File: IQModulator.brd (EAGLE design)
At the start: 100 x 80 mm, 122 parts, among them IC1 LM340S, IC2 OP470D, IC3 4539D, IC5 FT232RL-FULLSSOP, IC6 74AC74D, IC7 SI5351A_DEVICE_SMD, IC8 MEGA8-AI, Q1 16MHz, Q2 25MHz, X1 KLBR4

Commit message: Filter + Lib
All Filters designed+ Eagle Lib extended
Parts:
- removed R20, R21, R24, R25: 45, resistor:R0805
- added IC4: SN74CBTLV3253D, _Bachelor-IQModulator:SO16
- C28, C30: value (none) -> 2.2n
- C29, C36, C38: value (none) -> 3.3n
- C31: value (none) -> 100p
- C37, C44, C46: value (none) -> 6.8n
- C39: value (none) -> 150p
- C45: value (none) -> 10n
- C47: value (none) -> 220p
- L11, L12: value (none) -> 4.7u
- L13, L14: value (none) -> 10u
- L15, L16: value (none) -> 15u
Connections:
- removed net N$24: C9.-, R20.1
- removed net N$25: C10.-, R21.1
- removed net N$38: C12.-, R25.1
- removed net N$40: C11.-, R24.1
- new net VDD: IC4.16
- new net VSS: IC4.8
- net -I: now also C12.-, IC4.13, IC4.3; no longer IC3.13, IC3.3, R25.2
- net -Q: now also C10.-, IC4.12, IC4.4; no longer IC3.12, IC3.4, R21.2
- net CLK1: now also IC4.14; no longer IC3.14
- net CLK2: now also IC4.2; no longer IC3.2
- net GND: now also IC4.1, IC4.15; no longer IC3.1, IC3.15
- net I: now also C11.-, IC4.10, IC4.6; no longer IC3.10, IC3.6, R24.2
- net N$16: now also IC4.7; no longer IC3.7
- net N$17: now also IC4.9; no longer IC3.9
- net Q: now also C9.-, IC4.11, IC4.5; no longer IC3.11, IC3.5, R20.2

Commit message: PA+ Relais
Added last changes in the main schematic
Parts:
- removed C49: 100n, resistor:C0805
- removed IC3: 4539D, 45xx:SO16
- added C61: 100n, resistor:C0805
- added C62: 4.7u, resistor:C0805
- added C63: 100n, _Bachelor-IQModulator:C0805
- added D1, D2, D3, D4, D5, D6, D7, D8: (no value), diode:DO214AA
- added L19, L20, L22: 10u, _Bachelor-IQModulator:L0805
- added L21: 30n, _Bachelor-IQModulator:L0805
- added R17, R18: 100, resistor:R0805
- added R20, R21, R25: 5, _Bachelor-IQModulator:R0805
- added R24: 0.5, _Bachelor-IQModulator:R0805
- added R29: 120, _Bachelor-IQModulator:R0805
- added R30: 90, _Bachelor-IQModulator:R0805
- added T1, T2, T3, T4, T5, T6, T7, T8: (no value), zetex:SOT-23
- added U$10, U$11, U$12, U$13, U$14, U$15, U$16, U$3, U$4, U$5, U$6, U$7, U$8, U$9: REED_REL, _Bachelor-IQModulator:REED_RELAY
- added U$17, U$18, U$19: NESG260234, _Bachelor-IQModulator:SOT-89
- added U$20, U$21: TRAFO_MID_ZAPF, _Bachelor-IQModulator:TRAFO_MID_ZAPF
- added U$22: RS_BNC_PCB, _Bachelor-IQModulator:COAX-RS
- C1: value 47u -> 1u; device resistor:C0805 -> _Bachelor-IQModulator:C0805
- C13: value 4.7u -> 1u
- C2: value 47u -> 100n; device resistor:PANASONIC_C -> _Bachelor-IQModulator:C0805
- IC1: value LM340S -> LP2992; device linear:SOT223 -> _Bachelor-IQModulator:SOT-23-5
- L1, L10, L11, L12, L13, L14, L2, L3, L4, L5, L6, L7, L8, L9: device _Bachelor_IQ_Mischer:L1008 -> _Bachelor-IQModulator:L0805
- L17: value (none) -> 30n; device _Bachelor_IQ_Mischer:L1008 -> _Bachelor-IQModulator:L0805
- L18: value (none) -> 10u
- R11, R12: value 5k -> 0.5; device resistor:R0805 -> _Bachelor-IQModulator:R0805
- R2, R3: value 13k -> 15k
- U$1, U$2: value MAX4734 -> REED_REL; device _Bachelor_IQ_Mischer:UMAX -> _Bachelor-IQModulator:REED_RELAY
- moved IC1 1070.4 mm to (-373.4, -986.8)
- moved C1 1037.8 mm to (-353.1, -966.5)
- moved R11 834.1 mm to (-344.2, -899.2)
- moved R12 833.0 mm to (-344.2, -904.2)
- moved C13 724.1 mm to (-320.0, -802.6)
- moved U$2 531.2 mm to (-306.1, -690.9)
- moved U$1 526.7 mm to (-306.1, -682.0)
- moved C2 398.1 mm to (-353.1, -986.8)
- moved L17 362.9 mm to (-354.3, -948.7)
- moved C55 322.5 mm to (-320.0, -892.8)
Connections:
- removed net MIX_OUT: C49.2, U$1.8
- removed net N$42: C4.2, JP2.1
- removed net N$45: C60.+, IC1.1, L18.P$2
- removed net VDD: IC4.16
- removed net VSS: IC4.8
- new net CONTROL1: IC8.32, T1.3
- new net CONTROL2: IC8.1, T2.3
- new net CONTROL3: IC8.2, T3.3
- new net CONTROL4: IC8.9, T4.3
- new net CONTROL5: IC8.10, T5.3
- new net CONTROL6: IC8.11, T6.3
- new net CONTROL7: IC8.12, T7.3
- new net CONTROL8: IC8.13, T8.3
- new net N$24: D1.C, T1.2, U$1.2, U$9.3
- new net N$25: C4.2, JP2.2
- new net N$38: D2.C, T2.2, U$10.3, U$2.2
- new net N$40: D4.C, T4.2, U$12.3, U$4.2
- new net N$46: D3.C, T3.2, U$11.3, U$3.2
- new net N$48: D5.C, T5.2, U$13.3, U$5.2
- new net N$50: D6.C, T6.2, U$14.3, U$6.2
- new net N$52: D7.C, T7.2, U$15.3, U$7.2
- new net N$54: D8.C, T8.2, U$16.3, U$8.2
- new net N$56: R12.2, U$18.C
- new net N$57: U$17.E, U$21.SECONDARY1
- new net N$58: U$18.E, U$21.SECONDARY2
- new net N$59: R21.1, R30.2, U$17.B
- new net N$60: R20.1, R30.1, U$18.B
- new net N$61: R24.2, U$19.C
- new net N$62: R25.1, U$19.B
- new net N$63: C2.1, R25.2, R29.2, U$19.E, U$20.SECONDARY_MID
- new net N$64: L21.P$2, R20.2
- new net N$65: L17.P$2, R21.2
- new net N$66: L21.P$1, U$20.SECONDARY1
- new net N$67: L17.P$1, U$20.SECONDARY2
- new net N$68: C1.1, L22.P$1, U$21.SECONDARY_MID
- new net N$69: C60.+, IC1.1, IC1.3, L18.P$2
- new net PA_IN: R13.1, R14.1, U$20.PRIMARY_TOP
- new net PA_OUT: U$1.1, U$2.1, U$21.PRIMARY_TOP, U$22.MID, U$3.1, U$4.1, U$5.1, U$6.1, U$7.1, U$8.1
- net +3V3: now also C13.2, C55.1, C62.1, IC1.5, IC4.16, L19.P$1, L20.P$1, L22.P$2, R29.1; no longer C1.1, C16.1, C17.2, IC1.3, IC3.16, IC7.1, IC7.7, R11.2, U$1.6, U$2.6
- net +5V: now also C59.+, IC5.4, L18.P$1, T1.1, T2.1, T3.1, T4.1, T5.1, T6.1, T7.1, T8.1; no longer C2.+, L17.P$1
- net BIAS: now also C61.2, R18.2; no longer C13.1, R11.1, R12.2
- net CLK1: now also IC4.2; no longer IC4.14
- net CLK2: now also IC4.14; no longer IC4.2
- net DTR: now also IC5.2; no longer C55.1
- net FIL1_OUT: now also U$9.1; no longer U$2.2
- net FIL2_OUT: now also U$10.1; no longer U$2.9
- net FIL3_OUT: now also U$11.1; no longer U$2.4
- net FIL4_OUT: now also U$12.1; no longer U$2.7
- net FIL5_OUT: now also U$13.1
- net FIL6_OUT: now also U$14.1
- net FIL7_OUT: now also U$15.1
- net FIL8_OUT: now also U$16.1
- net FILTER1: now also U$1.4; no longer U$1.2
- net FILTER2: now also U$2.4; no longer U$1.9
- net FILTER3: now also U$3.4; no longer U$1.4
- net FILTER4: now also U$4.4; no longer U$1.7
- net FILTER5: now also U$5.4
- net FILTER6: now also U$6.4
- net FILTER7: now also U$7.4
- net FILTER8: now also U$8.4
- net GND: now also C13.1, C2.2, C55.2, C61.1, C62.2, C63.1, D1.A, D2.A, D3.A, D4.A, D5.A, D6.A, D7.A, D8.A, IC4.8, JP2.1, R11.1, R24.1, U$10.2, U$11.2, U$12.2, U$13.2, U$14.2, U$15.2, U$16.2, U$21.PRIMARY_BOTTOM, U$22.P$1, U$22.P$2, U$22.P$3, U$22.P$4, U$3.3, U$4.3, U$5.3, U$6.3, U$7.3, U$8.3, U$9.2, U1.GND1; no longer C13.2, C2.-, C4.1, IC1.4, IC3.8
- net I_IN: now also C3.-; no longer C3.+
- net N$1: now also C57.2, R17.1, R28.2; no longer IC5.4
- net N$2: now also C3.+; no longer C3.-
- net N$26: now also R19.1, S1.2; no longer U1.GND1
- net N$30: now also C16.1, IC7.1, L20.P$2; no longer C55.2, IC5.2
- net N$36: now also R18.1
- net N$39: now also C17.2, IC7.7, L19.P$2; no longer U$2.8
- net N$4: now also C58.+; no longer C58.-
- net N$44: now also R11.2, U$17.C; no longer C59.+, L17.P$2, L18.P$1
- net OFFSET: now also C63.2, R17.2, U$20.PRIMARY_BOTTOM; no longer C49.1, C57.2, R13.1, R14.1, R28.2
- net Q_IN: now also C58.-; no longer C58.+
- net RESET: now also C4.1; no longer JP2.2

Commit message: Beta V. 0.1
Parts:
- removed U1: (no value), MicroUSB:USB-MICRO-SMD
- added C49: 1u, resistor:C0805
- added C64: 100n, resistor:C0805
- added C65: 10n, resistor:C0805
- added C66, C67: 1p, _Bachelor-IQModulator:C0805
- added K1: (no value), Input-Output_Connectors_rev15d:629105150521
- C53: value 0.1u -> 100n
- R17: value 100 -> 500
- X2: value (none) -> CLK2
- renumbered X3 to CLK3
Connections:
- new net LOAD: U$10.4, U$11.4, U$12.4, U$13.4, U$14.4, U$15.4, U$16.4, U$22.MID, U$9.4
- new net N$42: C65.1, IC1.4
- net +3V3: now also C49.1, C64.2
- net +5V: now also K1.1; no longer U1.VBUS1
- net D+: now also K1.3; no longer U1.D+1
- net D-: now also K1.2; no longer U1.D-1
- net GND: now also C49.2, C64.1, C65.2, K1.5, K1.Z1, K1.Z2, K1.Z3, K1.Z4; no longer U1.GND1
- net N$57: now also C66.2
- net N$58: now also C67.1
- net N$59: now also C67.2
- net N$60: now also C66.1
- net PA_OUT: no longer U$22.MID

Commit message: Started with Layout
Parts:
- removed C61: 100n, resistor:C0805
- removed L20: 10u, _Bachelor-IQModulator:L0805
- removed R18: 100, resistor:R0805
- added C68: 470u, resistor:PANASONIC_D
- added C69, C75: 100n, resistor:C0805
- added C70, C71: 1p, _Bachelor-IQModulator:C0805
- added C72, C73: 47u, resistor:PANASONIC_C
- added C74: 4.7u, resistor:C0805
- added JP3: (no value), jumper:JP2
- added R31, R32: 4.7k, resistor:R0805
- added R33: 100, resistor:R0805
- IC2: value OP470D -> TLV2464CDD; device linear:SO14 -> _Bachelor-IQModulator:SO14
- L19: device _Bachelor-IQModulator:L0805 -> _Bachelor_IQ_Mischer:L1008
- moved C65 1226.2 mm to (140.3, 69.2), turned to 180 degrees
- moved C64 1216.0 mm to (121.9, 78.7), turned to 90 degrees
- moved C67 1209.0 mm to (140.3, 37.5), turned to 90 degrees
- moved C66 1200.2 mm to (123.8, 41.9), turned to 180 degrees
- moved C62 1194.8 mm to (150.5, 80.0), turned to 180 degrees
- moved IC1 1185.3 mm to (154.9, 74.3), turned to 90 degrees
- moved K1 1175.0 mm to (156.8, 15.2), turned to 90 degrees
- moved U$22 1172.2 mm to (29.8, 90.8)
- moved C49 1166.6 mm to (88.3, 46.0)
- moved R17 1164.4 mm to (93.2, 47.8)
- moved C63 1154.7 mm to (108.0, 49.5), turned to 90 degrees
- moved C2 1147.5 mm to (141.0, 48.9), turned to 270 degrees
- moved U$20 1144.8 mm to (128.3, 55.9)
- moved L21 1124.7 mm to (134.6, 59.1)
- moved U$21 1112.0 mm to (79.4, 39.1)
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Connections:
- removed net N$24: D1.C, T1.2, U$1.2, U$9.3
- removed net N$50: D6.C, T6.2, U$14.3, U$6.2
- removed net N$52: D7.C, T7.2, U$15.3, U$7.2
- new net CLEAN_5V: C73.+, JP3.3, L19.P$2
- new net N$43: D4.A, T4.1, U$12.2, U$4.3
- new net N$45: D3.A, T3.1, U$11.2, U$3.3
- new net N$47: D2.A, T2.1, U$10.2, U$2.3
- new net N$49: C70.2, U$21.SECONDARY2
- new net N$51: C74.2, R31.1, R32.2, R33.1
- net +3V3: now also C16.1, C17.2, IC7.1, IC7.7, JP3.1; no longer C64.2, IC2.4, L19.P$1, L20.P$1
- net +5V: now also C69.1, C72.+, D1.C, D2.C, D3.C, D4.C, D5.C, D6.C, D7.C, D8.C, L19.P$1, U$1.2, U$10.3, U$11.3, U$12.3, U$13.3, U$14.3, U$15.3, U$16.3, U$2.2, U$3.2, U$4.2, U$5.2, U$6.2, U$7.2, U$8.2, U$9.3; no longer T1.1, T2.1, T3.1, T4.1, T5.1, T6.1, T7.1, T8.1
- net BIAS: now also C75.2, R33.2; no longer C61.2, R18.2
- net GND: now also C68.-, C69.2, C72.-, C73.-, C74.1, C75.1, R32.1, T1.2, T2.2, T3.2, T4.2, T5.2, T6.2, T7.2, T8.2; no longer C61.1, D1.A, D2.A, D3.A, D4.A, D5.A, D6.A, D7.A, D8.A, U$1.3, U$10.2, U$11.2, U$12.2, U$13.2, U$14.2, U$15.2, U$16.2, U$2.3, U$3.3, U$4.3, U$5.3, U$6.3, U$7.3, U$8.3, U$9.2
- net N$30: now also D6.A, T6.1, U$14.2, U$6.3; no longer C16.1, IC7.1, L20.P$2
- net N$36: no longer R18.1
- net N$38: now also D1.A, T1.1, U$1.3, U$9.2; no longer D2.C, T2.2, U$10.3, U$2.2
- net N$39: now also D5.A, T5.1, U$13.2, U$5.3; no longer C17.2, IC7.7, L19.P$2
- net N$40: now also D7.A, T7.1, U$15.2, U$7.3; no longer D4.C, T4.2, U$12.3, U$4.2
- net N$46: now also D8.A, T8.1, U$16.2, U$8.3; no longer D3.C, T3.2, U$11.3, U$3.2
- net N$48: now also C71.1, U$21.SECONDARY1; no longer D5.C, T5.2, U$13.3, U$5.2
- net N$54: now also C64.2, IC2.4, JP3.2, R31.2; no longer D8.C, T8.2, U$16.3, U$8.2
- net N$57: now also C71.2; no longer U$21.SECONDARY1
- net N$58: now also C70.1; no longer U$21.SECONDARY2
- net OFFSET: now also C68.+
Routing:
- added copper zone on layer 1, net GND
- added copper zone on layer 16, net GND
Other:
- board size 100 x 80 mm -> 160 x 100 mm

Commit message: advanced Layout
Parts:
- moved C16 59.0 mm to (81.9, 8.89), turned to 0 degrees
- moved C52 58.8 mm to (125.7, 31.8), turned to 90 degrees
- moved CLK3 48.9 mm to (72.4, 5.08)
- moved C17 47.7 mm to (85.1, 19.7), turned to 270 degrees
- moved C53 46.9 mm to (118.1, 10.2)
- moved IC8 45.8 mm to (121.8, 19.6)
- moved C54 44.4 mm to (121.3, 10.2)
- moved IC7 43.8 mm to (81.9, 15.2)
- moved T1 42.1 mm to (19.1, 85.1), turned to 270 degrees
- moved C50 39.5 mm to (108.0, 31.2), turned to 90 degrees
- moved X2 39.4 mm to (91.4, 5.08)
- moved C51 39.0 mm to (122.7, 31.6), turned to 90 degrees
- moved Q1 39.0 mm to (115.6, 30.5)
- moved T2 38.4 mm to (19.1, 74.3), turned to 270 degrees
- moved U$22 36.9 mm to (66.7, 92.1)
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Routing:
- net +3V3: track 0.00 -> 89.1 mm, vias 0 -> 6
- net SDA: track 0.00 -> 78.1 mm, vias 0 -> 6
- net UC_VCC: track 0.00 -> 70.2 mm, vias 0 -> 2
- net SCL: track 0.00 -> 56.7 mm, vias 0 -> 2
- net PB3: track 0.00 -> 54.8 mm, vias 0 -> 2
- net PB4: track 0.00 -> 54.6 mm, vias 0 -> 1
- net CLK2: track 0.00 -> 53.1 mm, vias 0 -> 2
- net CONTROL5: track 0.00 -> 50.3 mm, vias 0 -> 1
- net +5V: track 0.00 -> 50.0 mm
- net PB5: track 0.00 -> 48.1 mm, vias 0 -> 2
- net CONTROL4: track 0.00 -> 47.5 mm, vias 0 -> 1
- net CLK1: track 0.00 -> 45.8 mm, vias 0 -> 1
- net RESET: track 0.00 -> 42.8 mm, vias 0 -> 4
- net CONTROL8: track 0.00 -> 36.0 mm, vias 0 -> 1
- net CONTROL7: track 0.00 -> 32.4 mm, vias 0 -> 1
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
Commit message: updated board
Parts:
- added R18: 0, resistor:R0805
- moved U$22 53.6 mm to (13.3, 86.4)
- moved C22 17.6 mm to (40.0, 85.7)
- moved D1 17.3 mm to (29.8, 97.2)
- moved T1 16.8 mm to (35.6, 88.3), turned to 180 degrees
- moved U$9 16.8 mm to (21.6, 94.6)
- moved U$10 16.7 mm to (21.0, 85.7)
- moved T2 16.7 mm to (34.9, 79.4), turned to 180 degrees
- moved L4 16.5 mm to (43.8, 87.0)
- moved C18 15.9 mm to (39.4, 94.6)
- moved D2 15.3 mm to (27.3, 87.6)
- moved C21 14.6 mm to (47.6, 86.4)
- moved L2 13.1 mm to (43.8, 95.2)
- moved C19 11.8 mm to (53.3, 92.1)
- moved L1 11.8 mm to (53.3, 95.2)
- moved C15 11.8 mm to (48.3, 94.0)
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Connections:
- net GND: now also R18.1, R18.2
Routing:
- net CLEAN_5V: track 0.00 -> 50.0 mm, vias 0 -> 1
- net +3V3: track 89.1 -> 134.9 mm
- net +5V: track 50.0 -> 77.5 mm
- net N$69: track 0.00 -> 18.7 mm
- net N$3: track 0.00 -> 16.6 mm
- net N$51: track 0.00 -> 16.1 mm
- net N$8: track 0.00 -> 8.46 mm
- net CLK1: track 45.8 -> 38.4 mm, vias 1 -> 2
- net Q: track 0.00 -> 7.41 mm
- net -Q: track 0.00 -> 6.67 mm
- net -I: track 0.00 -> 6.67 mm
- net CLK2: track 53.1 -> 59.6 mm, vias 2 -> 3
- net BIAS: track 0.00 -> 4.90 mm
- net N$42: track 0.00 -> 4.86 mm
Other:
- board size 160 x 100 mm -> 160 x 99.7 mm

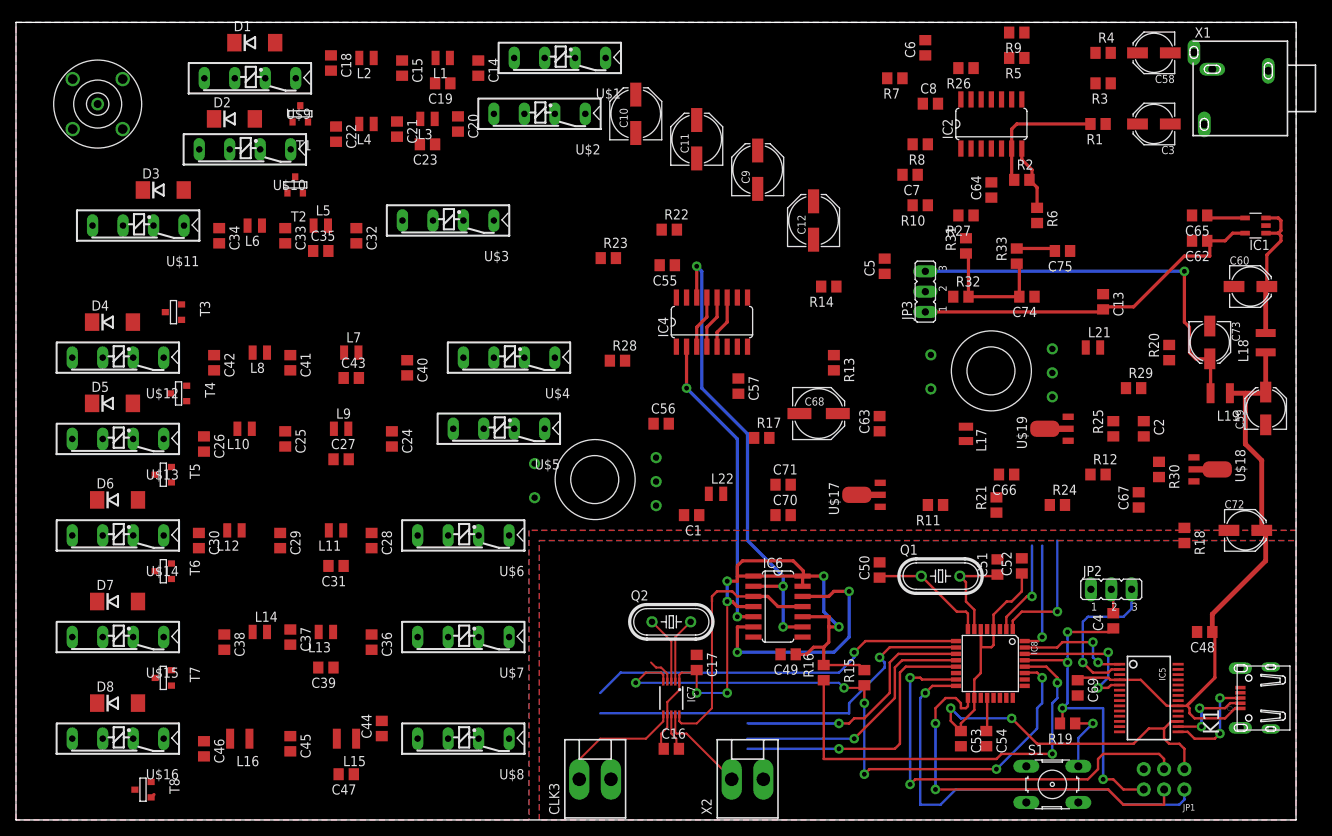
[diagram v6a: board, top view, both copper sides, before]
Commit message: Board smaller now!
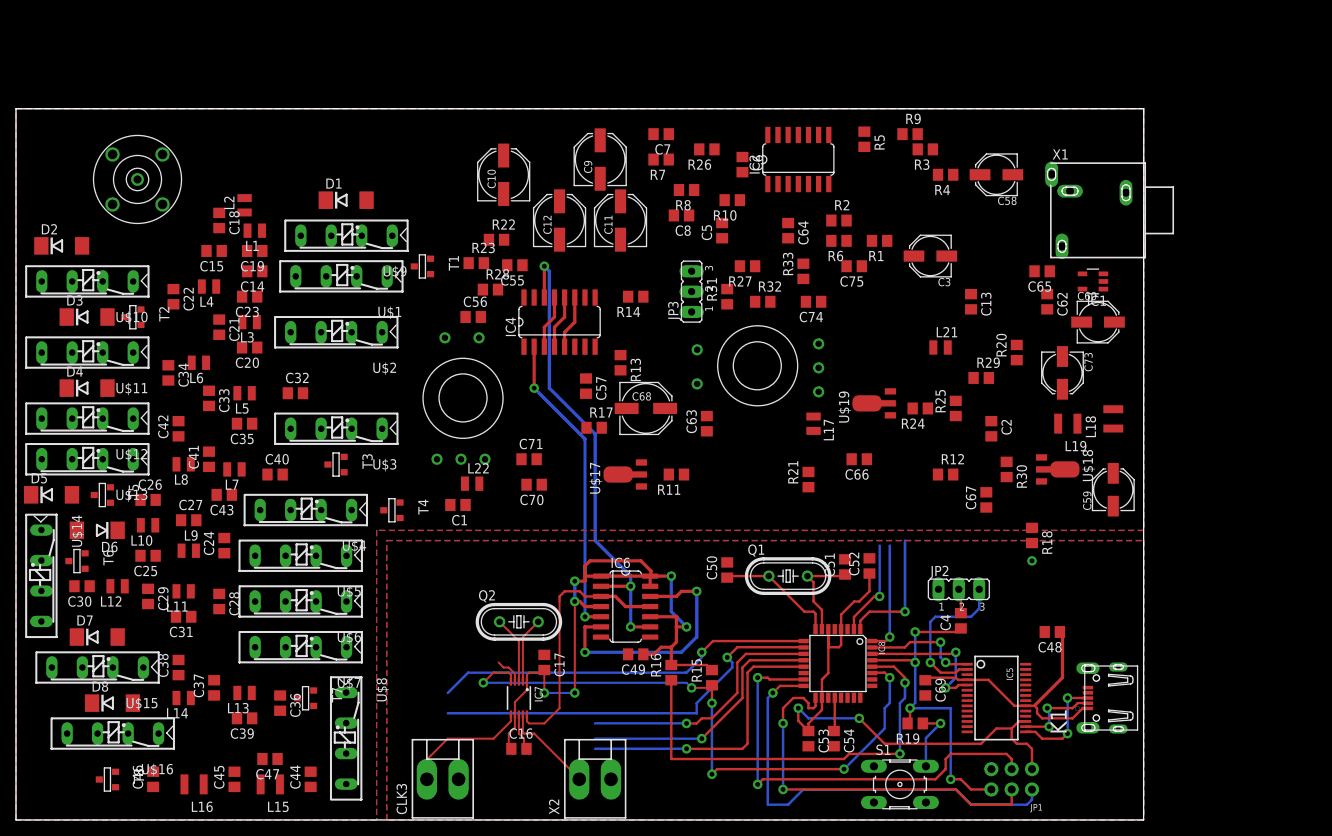
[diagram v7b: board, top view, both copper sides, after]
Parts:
- removed C72: 47u, resistor:PANASONIC_C
- moved U$1 38.6 mm to (33.0, 69.8)
- moved C20 38.2 mm to (29.2, 59.1), turned to 180 degrees
- moved C14 37.8 mm to (29.8, 68.6), turned to 180 degrees
- moved U$2 37.3 mm to (32.4, 62.9)
- moved C8 34.1 mm to (83.2, 75.6), turned to 180 degrees
- moved R26 33.9 mm to (86.4, 83.8)
- moved L3 33.8 mm to (29.2, 62.2)
- moved C21 33.3 mm to (25.4, 61.6)
- moved C15 32.8 mm to (24.8, 71.1), turned to 180 degrees
- moved R11 32.6 mm to (82.5, 43.2)
- moved C3 32.5 mm to (114.3, 70.5)
- moved L1 31.9 mm to (29.8, 73.7)
- moved C71 31.9 mm to (64.1, 45.1)
- moved C12 31.8 mm to (67.9, 74.9)
- moved U$4 31.7 mm to (28.6, 40.6)
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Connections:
- net +5V: no longer C72.+
- net GND: no longer C72.-
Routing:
- net CLEAN_5V: track 50.0 -> 0.00 mm, vias 1 -> 0
- net +3V3: track 134.9 -> 89.1 mm
- net +5V: track 77.5 -> 34.4 mm
- net N$69: track 18.7 -> 0.00 mm
- net N$3: track 16.6 -> 0.00 mm
- net N$51: track 16.1 -> 0.00 mm
- net N$8: track 8.46 -> 0.00 mm
- net BIAS: track 4.90 -> 0.00 mm
- net N$42: track 4.86 -> 0.00 mm
- net CONTROL8: track 36.0 -> 35.5 mm
- net GND: vias 0 -> 1
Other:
- board size 160 x 99.7 mm -> 141 x 88.9 mm

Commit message: Close to finish
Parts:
- moved C55 58.6 mm to (120.8, 64.6), turned to 90 degrees
- moved C13 57.3 mm to (62.2, 69.2), turned to 0 degrees
- moved C64 6.38 mm to (97.2, 67.3), turned to 90 degrees
- moved IC2 6.35 mm to (97.8, 76.2)
- moved R3 5.08 mm to (113.7, 78.7)
- moved R2 4.96 mm to (106.0, 71.1), turned to 180 degrees
- moved R4 4.49 mm to (115.6, 76.2)
- moved R1 4.45 mm to (108.0, 67.9)
- moved R9 4.26 mm to (113.7, 81.9)
- moved C6 3.81 mm to (90.8, 85.7), turned to 90 degrees
- moved R6 3.42 mm to (106.0, 73.7), turned to 0 degrees
- moved C70 2.84 mm to (67.3, 40.6), turned to 90 degrees
- moved C3 2.54 mm to (114.3, 67.9)
- moved C75 2.29 mm to (102.9, 67.9)
- moved R33 2.01 mm to (99.1, 66.7)
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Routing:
- net +3V3: track 89.1 -> 227.3 mm, vias 6 -> 10
- net N$58: track 0.00 -> 62.5 mm
- net CLEAN_5V: track 0.00 -> 61.3 mm, vias 0 -> 1
- net N$13: track 0.00 -> 61.0 mm, vias 0 -> 2
- net N$59: track 0.00 -> 47.9 mm
- net +5V: track 34.4 -> 82.1 mm
- net N$57: track 0.00 -> 39.6 mm
- net N$60: track 0.00 -> 34.9 mm
- net N$63: track 0.00 -> 34.3 mm
- net N$12: track 0.00 -> 31.5 mm, vias 0 -> 2
- net N$9: track 0.00 -> 26.4 mm, vias 0 -> 2
- net N$8: track 0.00 -> 26.3 mm, vias 0 -> 2
- net N$1: track 0.00 -> 25.2 mm
- net N$7: track 0.00 -> 23.7 mm
- net BIAS: track 0.00 -> 23.3 mm
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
